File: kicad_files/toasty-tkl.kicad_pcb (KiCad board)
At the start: 2 copper layers, 345.7 x 134.1 mm, 204 parts, among them CON1 USB-MINI-B, Q1 FET_N, SW0:0 ESC, SW0:10 F9, SW0:11 F10, SW0:12 F11, SW0:13 F12, SW0:14 PRINT, SW0:15 SCROLL LOCK, SW0:2 F1, SW0:3 F2, SW0:4 F3, SW0:5 F4, SW0:6 F5, SW0:7 F6, SW0:8 F7, SW0:9 F8, SW1:0 `, SW1:1 1, SW1:10 0, SW1:11 -, SW1:12 =, SW1:13 BACK SPACE, SW1:14 INSERT, SW1:15 HOME, SW1:2 2, SW1:3 3, SW1:4 4, SW1:5 5, SW1:6 6, SW1:7 7, SW1:8 8, SW1:9 9, SW2:0 TAB, SW2:1 Q, SW2:10 P, SW2:11 [, SW2:12 ], SW2:13 \, SW2:14 DELETE, SW2:15 END, SW2:2 W, SW2:3 E, SW2:4 R, SW2:5 T, SW2:6 Y, SW2:7 U, SW2:8 I, SW2:9 O, SW3:0 CAPS LOCK, SW3:1 A, SW3:10 ;, SW3:11 ', SW3:13 ENTER, SW3:14 PAGE UP, SW3:15 PAUSE, SW3:2 S, SW3:3 D, SW3:4 F, SW3:5 G, SW3:6 H, SW3:7 J, SW3:8 K, SW3:9 L, SW4:0 LEFT SHIFT, SW4:1 Z, SW4:10 /, SW4:13 RIGHT SHIFT, SW4:14 PAGE DOWN, SW4:15 UP, SW4:2 X, SW4:3 C, SW4:4 V, SW4:5 B, SW4:6 N, SW4:7 M, SW4:8 ,, SW4:9 ., SW5:0 LEFT CTRL, SW5:1 LEFT WINDOWS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

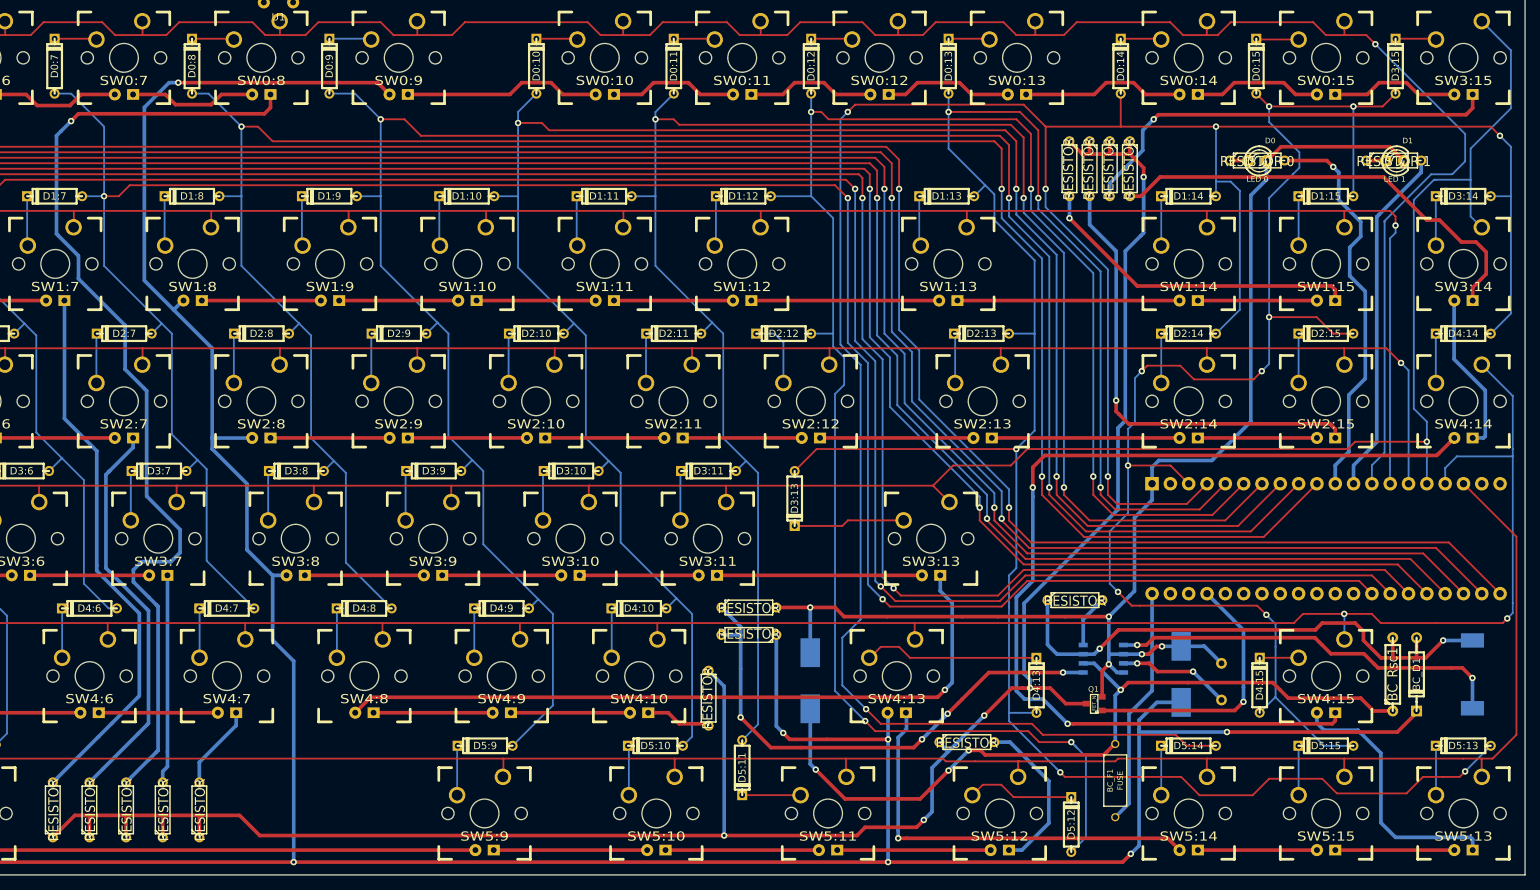
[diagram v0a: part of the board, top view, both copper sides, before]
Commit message: Finished parts list, fixed LED notes. double checked all parts, flipped boost converter parts all to rear of PCB.
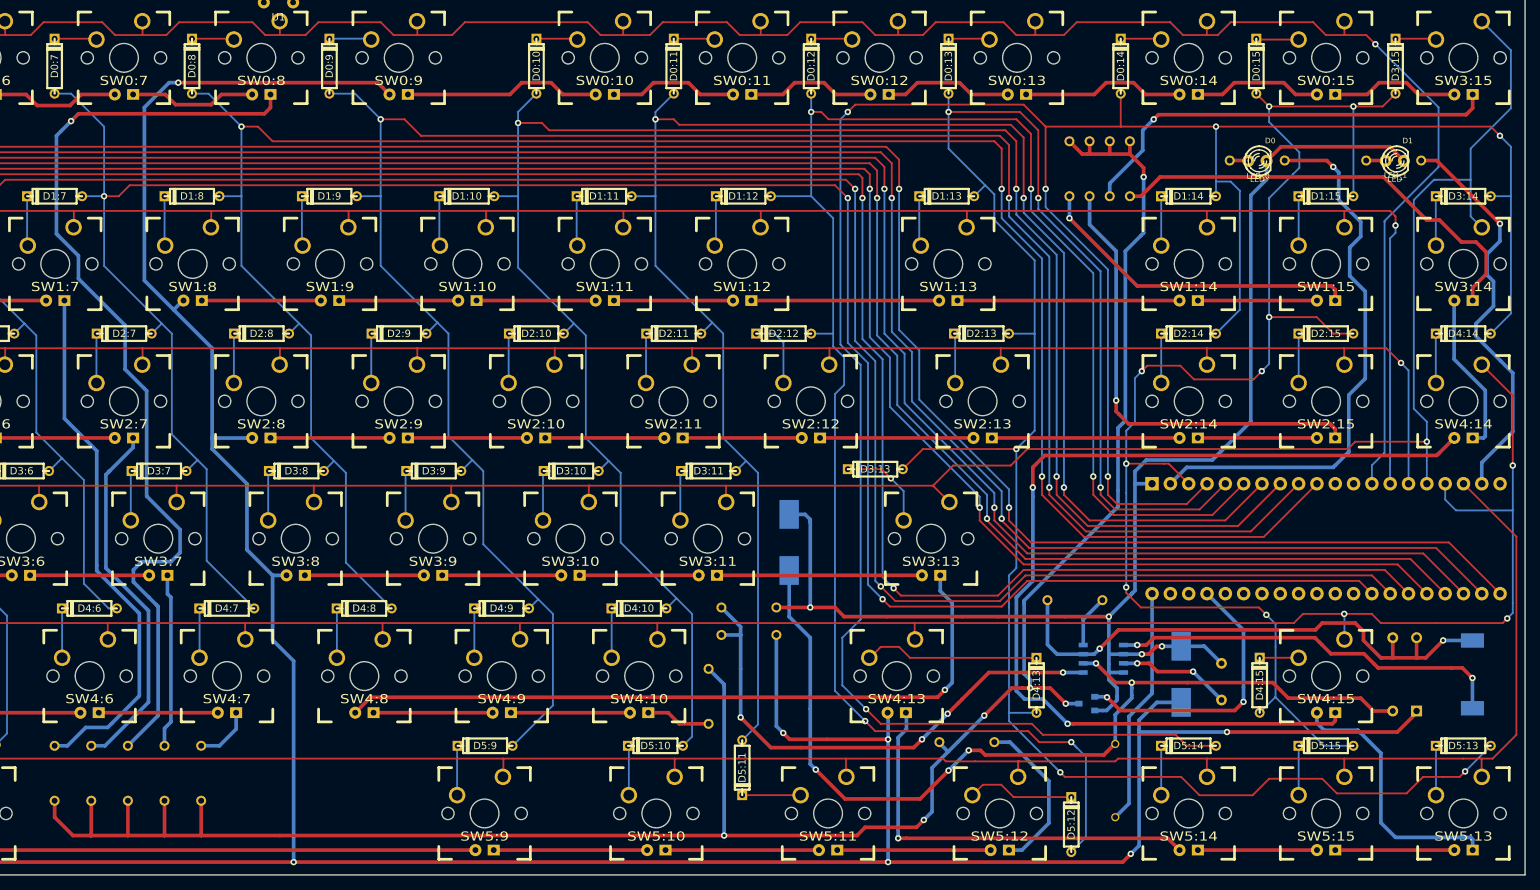
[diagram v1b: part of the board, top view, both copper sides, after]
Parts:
- removed R11, R12: RESISTOR, R3
- added LED_R0: RESISTOR, R3, B.Cu at (327.0, 40.5)
- added LED_R1: RESISTOR, R3, B.Cu at (345.9, 40.5)
- BC_D1, BC_F1, BC_R0, BC_R1, BC_R2, BC_Rsc1, Q1, R10, R2, R3, R4, R5, R6, R7, R8, R9: moved to B.Cu
- D0: value LED 0 -> LED
- D1: value LED 1 -> LED
- R0: value RESISTOR 0 -> RESISTOR; moved to B.Cu
- R1: value RESISTOR 1 -> RESISTOR; moved to B.Cu
- moved R1 204.2 mm to (160.3, 125.5), turned to 90 degrees
- moved R0 178.2 mm to (170.4, 125.5), turned to 90 degrees
- moved R6 166.7 mm to (301.0, 41.7), turned to 270 degrees
- moved R7 160.5 mm to (303.8, 41.7), turned to 270 degrees
- moved R5 122.0 mm to (286.8, 121.2), turned to 0 degrees
- moved R2 121.5 mm to (165.4, 125.5), turned to 90 degrees
- moved R9 90.2 mm to (251.0, 114.8)
- moved BC_Cvcc1 19.4 mm to (262.1, 93.5)
- moved D3:13 11.9 mm to (274.1, 83.3), turned to 180 degrees
- moved R4 7.37 mm to (180.6, 125.5)
- moved R3 7.01 mm to (175.5, 125.5)
- moved R8 5.59 mm to (306.6, 41.7)
- moved R10 2.79 mm to (309.4, 41.7)
- moved Q1 1.02 mm to (303.4, 115.8), turned to 270 degrees
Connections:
- R0 pad 1: N-0000075 -> N-0000071
- R0 pad 2: /LED 0 -> /LEDROW0
- R1 pad 1: N-0000076 -> N-0000071
- R1 pad 2: /LED 1 -> /LEDROW1
- R10 pad 2: /LEDROW8 -> /LEDROW10
- R2 pad 2: /LEDROW5 -> /LEDROW2
- R3 pad 2: /LEDROW4 -> /LEDROW3
- R4 pad 2: /LEDROW3 -> /LEDROW4
- R5 pad 2: /LEDROW2 -> /LEDROW5
- R6 pad 2: /LEDROW1 -> /LEDROW6
- R7 pad 2: /LEDROW0 -> /LEDROW7
- R8 pad 2: /LEDROW6 -> /LEDROW8
- R9 pad 2: /LEDROW7 -> /LEDROW9
- U0 pad 11: /LED 0 -> (no net)
- U0 pad 12: /LED 1 -> (no net)
- U0 pad 19: (no net) -> /LED 1
- U0 pad 2: (no net) -> /LED 0
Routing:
- net /LED 0: track 55.9 -> 77.2 mm
- net N-00000104: track 110.0 -> 131.1 mm, vias 4 -> 5
- net /GND: track 181.2 -> 197.6 mm, vias 5 -> 4
- net /COL 13: track 297.8 -> 282.7 mm
- net /LED 1: track 48.7 -> 56.6 mm, vias 0 -> 1
- net N-0000071: track 293.3 -> 300.6 mm, vias 5 -> 6
- net /LEDROW0: track 138.2 -> 133.0 mm
- net /LEDROW3: track 29.0 -> 24.2 mm
- net /ROW 0: track 435.1 -> 430.3 mm
- net /LEDROW2: track 56.5 -> 52.4 mm
- net /LEDROW4: track 11.8 -> 8.08 mm
- net N-00000149: track 15.4 -> 13.1 mm, vias 0 -> 1
- net /LEDROW1: track 76.1 -> 73.7 mm
- net /COL 15: track 197.6 -> 195.5 mm
- net N-00000105: track 37.2 -> 39.0 mm, vias 1 -> 2
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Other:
- board text added: "BC_Co1"
- board text added: "BC_Cvcc1"
- board text added: "BC_D1"
- board text added: "BC_F1 (FUSE)"
- board text added: "BC_R0"
- board text added: "BC_R1"
- board text added: "BC_R2"
- board text added: "BC_Rsc1"
- board text added: "LED_0"
- board text added: "LED_1"
- board text added: "LED_R0"
- board text added: "LED_R1"
- board text added: "R0"
- board text added: "R1"
- board text added: "R10"
- board text added: "R2"
- board text added: "R3"
- board text added: "R4"
- board text added: "R5"
- board text added: "R6"
- board text added: "R7"
- board text added: "R8"
- board text added: "R9"

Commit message: Added and fixed silk screen tags, added usb connector to part list.
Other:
- board text added: "D+"
- board text added: "D-"
- board text added: "F8"
- board text added: "GND"
- board text added: "ID"
- board text added: "VBUS"
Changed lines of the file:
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@@
     (links 408)
     (no_connects 0)
-    (area 18.416199 5.436799 364.234801 139.648001)
+    (area 3.963999 -151.103001 377.912301 568.094801)
     (thickness 1.6)
-    (drawings 277)
+    (drawings 282)
     (tracks 1865)
     (zones 0)
@@
     (25 Cmts.User user hide)
     (26 Eco1.User user hide)
-    (27 Eco2.User user)
+    (27 Eco2.User user hide)
     (28 Edge.Cuts user)
   )
   (setup
-    (last_trace_width 0.508)
+    (last_trace_width 0.254)
     (user_trace_width 0.508)
     (trace_clearance 0.254)
@@
     )
   )
+  (gr_text D- (at 193.294 17.145) (layer B.SilkS)
+    (effects (font (size 0.4572 0.4572) (thickness 0.0762)) (justify mirror))
+  )
+  (gr_text D+ (at 191.262 15.875) (layer B.SilkS)
+    (effects (font (size 0.4572 0.4572) (thickness 0.0762)) (justify mirror))
+  )
+  (gr_text ID (at 189.23 17.145) (layer B.SilkS)
+    (effects (font (size 0.4572 0.4572) (thickness 0.0762)) (justify mirror))
+  )
+  (gr_text GND (at 186.944 15.875) (layer B.SilkS)
+    (effects (font (size 0.4572 0.4572) (thickness 0.0762)) (justify mirror))
+  )
+  (gr_text VBUS (at 196.215 15.875) (layer B.SilkS)
+    (effects (font (size 0.4572 0.4572) (thickness 0.0762)) (justify mirror))
+  )
   (gr_text "BC_F1\n(FUSE)" (at 306.705 126.746 90) (layer B.SilkS)
     (effects (font (size 0.762 0.762) (thickness 0.1778)) (justify mirror))
@@
     (effects (font (size 1.5 1.5) (thickness 0.3)) (justify mirror))
   )
-  (gr_text END (at 344.424 73.914 90) (layer B.SilkS)
+  (gr_text END (at 328.676 73.914 90) (layer B.SilkS)
     (effects (font (size 1.5 1.5) (thickness 0.3)) (justify mirror))
   )
-  (gr_text HOME (at 344.678 54.864 90) (layer B.SilkS)
+  (gr_text HOME (at 328.676 54.864 90) (layer B.SilkS)
     (effects (font (size 1.5 1.5) (thickness 0.3)) (justify mirror))
   )
-  (gr_text DELETE (at 325.628 73.914 90) (layer B.SilkS)
+  (gr_text DELETE (at 309.245 73.787 90) (layer B.SilkS)
     (effects (font (size 1.5 1.5) (thickness 0.3)) (justify mirror))
   )
-  (gr_text INSERT (at 325.628 54.61 90) (layer B.SilkS)
+  (gr_text INSERT (at 309.372 54.991 90) (layer B.SilkS)
     (effects (font (size 1.5 1.5) (thickness 0.3)) (justify mirror))
   )
@@
     (effects (font (size 1.5 1.5) (thickness 0.3)) (justify mirror))
   )
-  (gr_text ] (at 261.62 64.77) (layer B.SilkS)
+  (gr_text ] (at 261.62 64.77 180) (layer B.SilkS)
     (effects (font (size 1.5 1.5) (thickness 0.3)) (justify mirror))
   )
-  (gr_text [ (at 246.38 64.77) (layer B.SilkS)
+  (gr_text [ (at 246.38 64.77 180) (layer B.SilkS)
     (effects (font (size 1.5 1.5) (thickness 0.3)) (justify mirror))
   )
@@
     (effects (font (size 1.5 1.5) (thickness 0.3)) (justify mirror))
   )
-  (gr_text F7 (at 199.898 27.686 90) (layer B.SilkS)
+  (gr_text F8 (at 199.898 27.686 90) (layer B.SilkS)
     (effects (font (size 1.5 1.5) (thickness 0.3)) (justify mirror))
   )
-  (gr_text F6 (at 180.848 27.94 90) (layer B.SilkS)
+  (gr_text F7 (at 180.848 27.94 90) (layer B.SilkS)
     (effects (font (size 1.5 1.5) (thickness 0.3)) (justify mirror))
   )
-  (gr_text F5 (at 161.798 27.686 90) (layer B.SilkS)
+  (gr_text F6 (at 161.798 27.686 90) (layer B.SilkS)
     (effects (font (size 1.5 1.5) (thickness 0.3)) (justify mirror))
   )

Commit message: Slight tweaks to silk screen and part list.
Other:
- board text added: "BC_Ct1"
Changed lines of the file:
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@@
-(kicad_pcb (version 3) (host pcbnew "(2013-04-19 BZR 4011)-stable")
+(kicad_pcb (version 3) (host pcbnew "(2013-05-31 BZR 4019)-stable")
   (general
     (links 408)
@@
     (area 3.963999 -151.103001 377.912301 568.094801)
     (thickness 1.6)
-    (drawings 282)
+    (drawings 283)
     (tracks 1865)
     (zones 0)
@@
       (usegerberextensions false)
       (excludeedgelayer true)
-      (linewidth 0)
+      (linewidth 0.150000)
       (plotframeref false)
       (viasonmask false)
@@
     )
   )
+  (gr_text BC_Ct1 (at 320.294 112.903 90) (layer B.SilkS)
+    (effects (font (size 0.762 0.762) (thickness 0.1778)) (justify mirror))
+  )
   (gr_text D- (at 193.294 17.145) (layer B.SilkS)
     (effects (font (size 0.4572 0.4572) (thickness 0.0762)) (justify mirror))
@@
     (effects (font (size 0.4572 0.4572) (thickness 0.0762)) (justify mirror))
   )
-  (gr_text "BC_F1\n(FUSE)" (at 306.705 126.746 90) (layer B.SilkS)
+  (gr_text "BC_F1\n(FUSE)" (at 303.276 126.619 90) (layer B.SilkS)
     (effects (font (size 0.762 0.762) (thickness 0.1778)) (justify mirror))
   )
@@
     (effects (font (size 0.762 0.762) (thickness 0.1778)) (justify mirror))
   )
-  (gr_text R10 (at 309.499 41.783 90) (layer B.SilkS)
+  (gr_text R10 (at 309.372 36.195) (layer B.SilkS)
     (effects (font (size 0.762 0.762) (thickness 0.1778)) (justify mirror))
   )
-  (gr_text R8 (at 306.705 41.783 90) (layer B.SilkS)
+  (gr_text R8 (at 306.578 36.195) (layer B.SilkS)
     (effects (font (size 0.762 0.762) (thickness 0.1778)) (justify mirror))
   )
-  (gr_text R7 (at 303.911 41.783 90) (layer B.SilkS)
+  (gr_text R7 (at 303.784 36.195) (layer B.SilkS)
     (effects (font (size 0.762 0.762) (thickness 0.1778)) (justify mirror))
   )
-  (gr_text R6 (at 301.117 41.783 90) (layer B.SilkS)
+  (gr_text R6 (at 300.99 36.195) (layer B.SilkS)
     (effects (font (size 0.762 0.762) (thickness 0.1778)) (justify mirror))
   )
-  (gr_text R1 (at 160.274 125.476 90) (layer B.SilkS)
+  (gr_text R1 (at 162.179 125.476 90) (layer B.SilkS)
     (effects (font (size 0.762 0.762) (thickness 0.1778)) (justify mirror))
   )
-  (gr_text R2 (at 165.354 125.476 90) (layer B.SilkS)
+  (gr_text R2 (at 167.259 125.476 90) (layer B.SilkS)
     (effects (font (size 0.762 0.762) (thickness 0.1778)) (justify mirror))
   )
-  (gr_text R0 (at 170.561 125.476 90) (layer B.SilkS)
+  (gr_text R0 (at 172.339 125.476 90) (layer B.SilkS)
     (effects (font (size 0.762 0.762) (thickness 0.1778)) (justify mirror))
   )
-  (gr_text R3 (at 175.641 125.476 90) (layer B.SilkS)
+  (gr_text R3 (at 177.419 125.476 90) (layer B.SilkS)
     (effects (font (size 0.762 0.762) (thickness 0.1778)) (justify mirror))
   )
-  (gr_text R4 (at 180.721 125.476 90) (layer B.SilkS)
+  (gr_text R4 (at 182.499 125.476 90) (layer B.SilkS)
     (effects (font (size 0.762 0.762) (thickness 0.1778)) (justify mirror))
   )
-  (gr_text R9 (at 251.079 114.935 90) (layer B.SilkS)
+  (gr_text R9 (at 250.952 109.474) (layer B.SilkS)
     (effects (font (size 0.762 0.762) (thickness 0.1778)) (justify mirror))
   )
-  (gr_text R5 (at 286.893 121.285) (layer B.SilkS)
+  (gr_text R5 (at 286.893 119.38) (layer B.SilkS)
     (effects (font (size 0.762 0.762) (thickness 0.1778)) (justify mirror))
   )
-  (gr_text BC_R0 (at 301.879 101.6) (layer B.SilkS)
+  (gr_text BC_R0 (at 301.879 99.695) (layer B.SilkS)
     (effects (font (size 0.762 0.762) (thickness 0.1778)) (justify mirror))
   )
-  (gr_text BC_D1 (at 349.123 111.506 90) (layer B.SilkS)
+  (gr_text BC_D1 (at 351.028 111.633 90) (layer B.SilkS)
     (effects (font (size 0.762 0.762) (thickness 0.1778)) (justify mirror))
   )
-  (gr_text BC_Rsc1 (at 345.821 111.887 90) (layer B.SilkS)
+  (gr_text BC_Rsc1 (at 343.916 111.76 90) (layer B.SilkS)
     (effects (font (size 0.762 0.762) (thickness 0.1778)) (justify mirror))
   )
@@
     (effects (font (size 0.762 0.762) (thickness 0.1778)) (justify mirror))
   )
-  (gr_text BC_R2 (at 256.667 106.299) (layer B.SilkS)
+  (gr_text BC_R2 (at 256.667 108.331) (layer B.SilkS)
     (effects (font (size 0.762 0.762) (thickness 0.1778)) (justify mirror))
   )
-  (gr_text BC_R1 (at 256.667 102.489) (layer B.SilkS)
+  (gr_text BC_R1 (at 256.667 104.394) (layer B.SilkS)
     (effects (font (size 0.762 0.762) (thickness 0.1778)) (justify mirror))
   )
@@
   (segment (start 300.355 103.759) (end 291.084 103.759) (width 0.508) (layer F.Cu) (net 17))
   (via (at 306.451 103.759) (size 0.889) (layers F.Cu B.Cu) (net 17))
-  (segment (start 319.532 107.87126) (end 319.70726 107.87126) (width 0.508) (layer B.Cu) (net 17))
-  (segment (start 319.70726 107.87126) (end 322.072 110.236) (width 0.508) (layer B.Cu) (net 17))
   (segment (start 311.9755 108.966) (end 311.023 108.966) (width 0.508) (layer F.Cu) (net 17))
   (segment (start 311.9755 108.966) (end 313.055 107.8865) (width 0.508) (layer F.Cu) (net 17))
@@
   (segment (start 269.748 103.759) (end 275.717 103.759) (width 0.508) (layer F.Cu) (net 17))
   (segment (start 268.478 102.489) (end 269.748 103.759) (width 0.508) (layer F.Cu) (net 17))
+  (segment (start 319.532 107.87126) (end 319.70726 107.87126) (width 0.508) (layer B.Cu) (net 17))
+  (segment (start 319.70726 107.87126) (end 322.072 110.236) (width 0.508) (layer B.Cu) (net 17))
   (segment (start 314.9854 85.3313) (end 314.9854 85.3186) (width 0.508) (layer B.Cu) (net 18))
   (segment (start 337.8454 82.7786) (end 339.725 80.899) (width 0.508) (layer B.Cu) (net 18))
@@
   (segment (start 300.101 111.506) (end 299.974 111.633) (width 0.254) (layer F.Cu) (net 210))
   (segment (start 299.974 111.633) (end 300.101 111.506) (width 0.254) (layer F.Cu) (net 210))
+  (via (at 318.135 111.379) (size 0.889) (layers F.Cu B.Cu) (net 211))
+  (segment (start 313.182 111.379) (end 318.135 111.379) (width 0.508) (layer F.Cu) (net 211))
+  (segment (start 322.072 115.316) (end 318.135 111.379) (width 0.508) (layer B.Cu) (net 211))
   (segment (start 311.9755 110.236) (end 312.039 110.236) (width 0.508) (layer F.Cu) (net 211))
   (via (at 310.388 110.236) (size 0.889) (layers F.Cu B.Cu) (net 211))
   (segment (start 308.483 110.236) (end 310.388 110.236) (width 0.508) (layer B.Cu) (net 211))
   (segment (start 311.9755 110.236) (end 310.388 110.236) (width 0.508) (layer F.Cu) (net 211))
-  (via (at 318.135 111.379) (size 0.889) (layers F.Cu B.Cu) (net 211))
-  (segment (start 313.182 111.379) (end 318.135 111.379) (width 0.508) (layer F.Cu) (net 211))
   (segment (start 312.039 110.236) (end 313.182 111.379) (width 0.508) (layer F.Cu) (net 211))
-  (segment (start 322.072 115.316) (end 318.135 111.379) (width 0.508) (layer B.Cu) (net 211))
   (segment (start 312.4454 114.4016) (end 309.245 117.602) (width 0.508) (layer B.Cu) (net 212))
   (segment (start 312.4454 114.0206) (end 312.4454 114.4016) (width 0.508) (layer B.Cu) (net 212))
